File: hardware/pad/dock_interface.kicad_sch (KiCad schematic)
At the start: 6 parts, among them J1 Pogo_6p, U1 TPD4E1U06DBVR

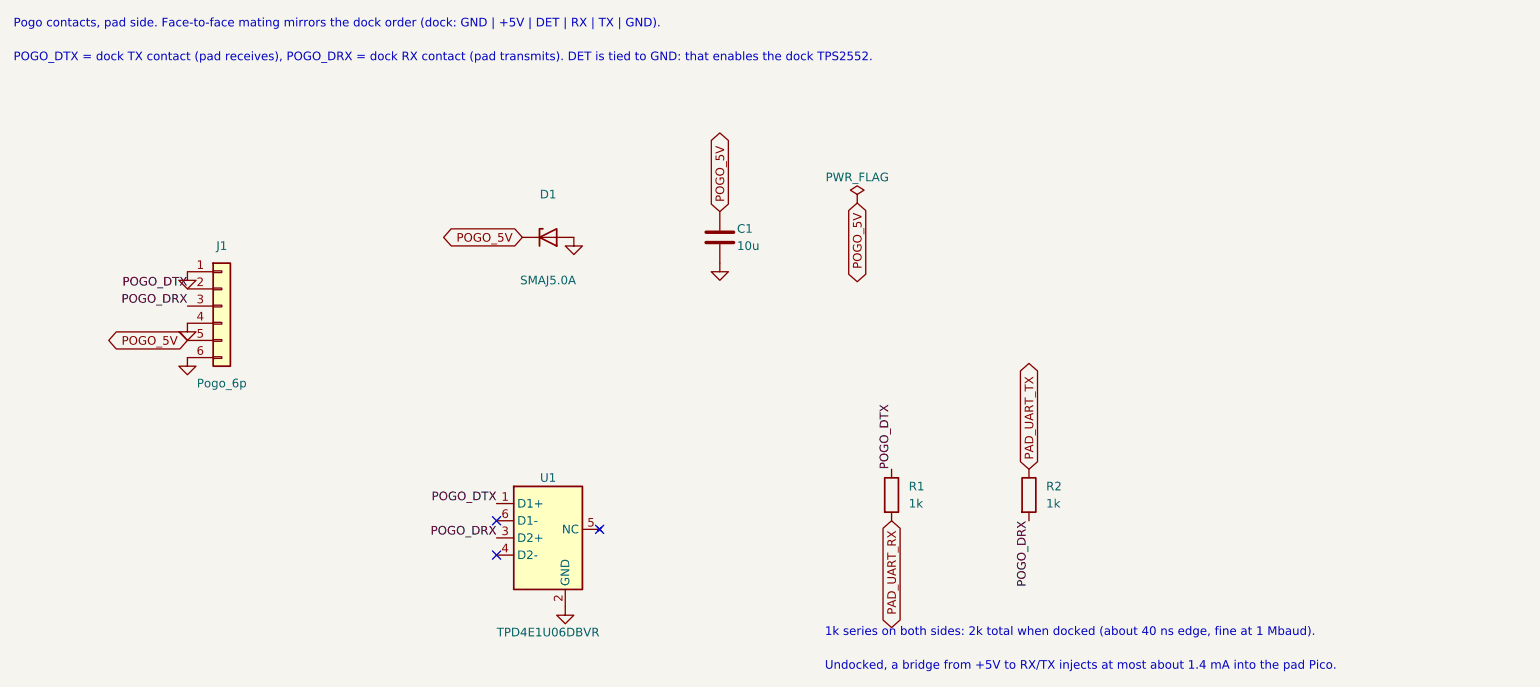
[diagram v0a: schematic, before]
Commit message: Pad schematic: hand-redrawn from the connection guide; netlist verified against the reference
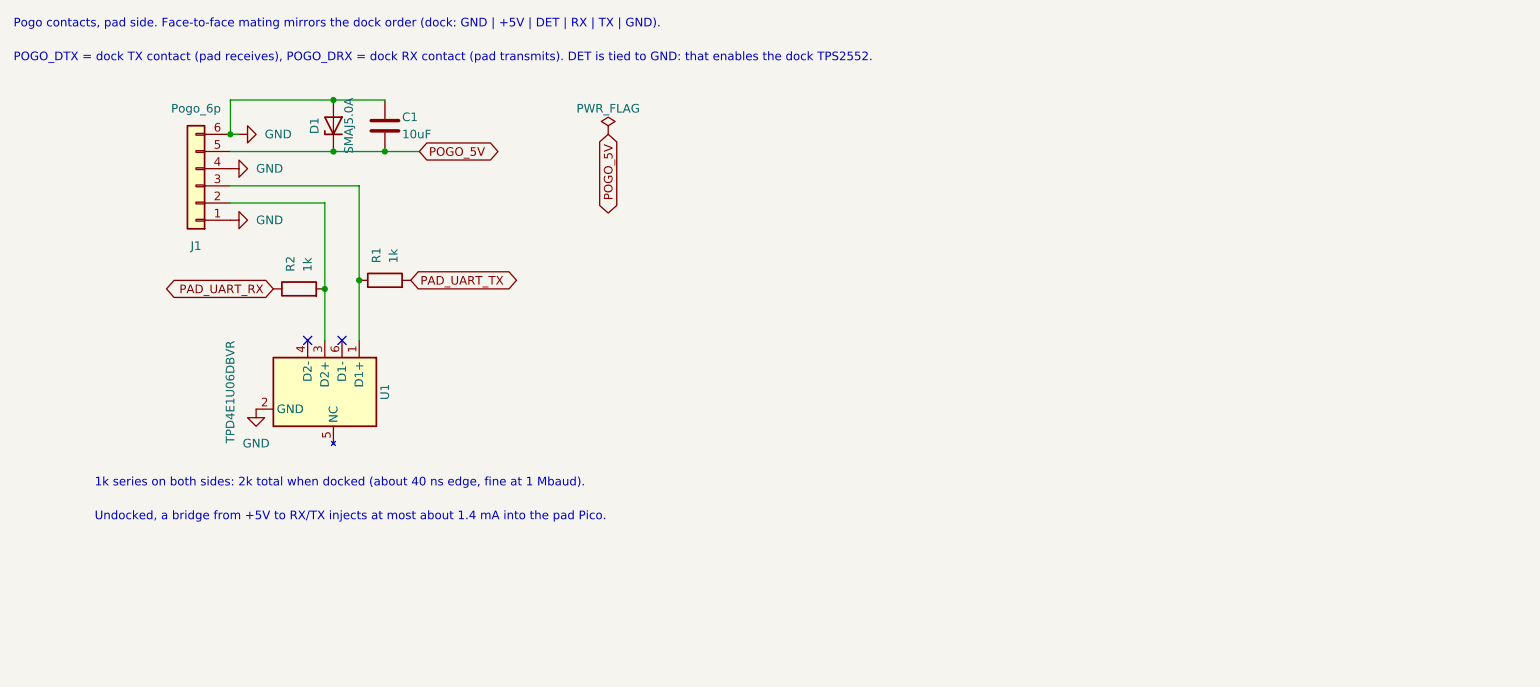
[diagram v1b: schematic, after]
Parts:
- C1: value 10u -> 10uF
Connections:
- net GND: now also C1.1; no longer C1.2
- net PAD_UART_RX: now also R2.1; no longer R1.2
- net PAD_UART_TX: now also R1.2; no longer R2.1
- net POGO_5V: now also C1.2; no longer C1.1
- net POGO_DRX: no longer names the net of R2.2, U1.3 (D2+)
- net POGO_DRX: now also J1.2 (Pin_2); no longer J1.3 (Pin_3)
- net POGO_DTX: no longer names the net of R1.1, U1.1 (D1+)
- net POGO_DTX: now also J1.3 (Pin_3); no longer J1.2 (Pin_2)
- no-connect marks 3 -> 2
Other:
- moved on the sheet: C1, D1, J1, U1
